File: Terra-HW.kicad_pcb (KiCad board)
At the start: 2 copper layers, 78.2 x 48.5 mm, 63 parts, among them J1 GT-USB-7010ASV, J2 S2B-PH-SM4-TB, J3 0532610271, J5 B8B-PH-SM4-TB, J6 0532610671, Q1 DMP3099L, Q2 2N7002, SW2 KMR231NG, SW3 KMR231NG, SW4 KMR231NG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

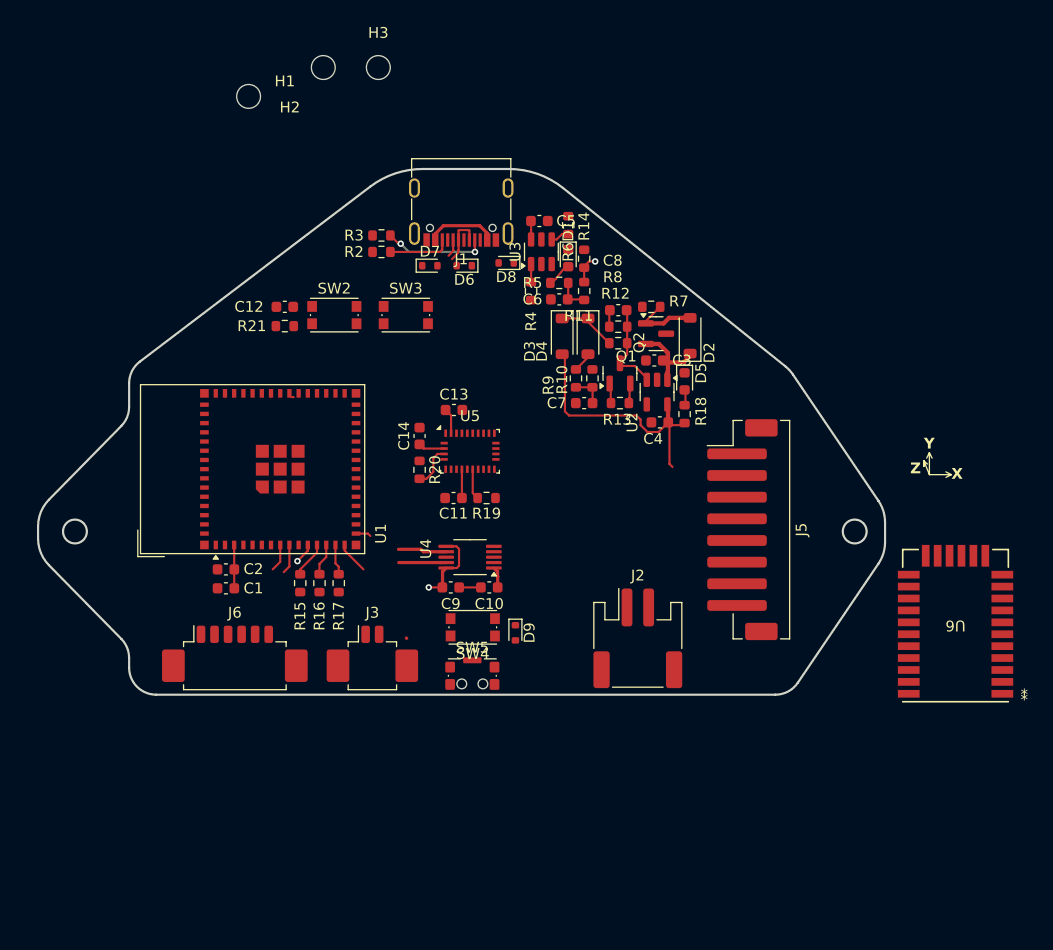
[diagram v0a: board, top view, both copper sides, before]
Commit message: Updated board outline to version 004
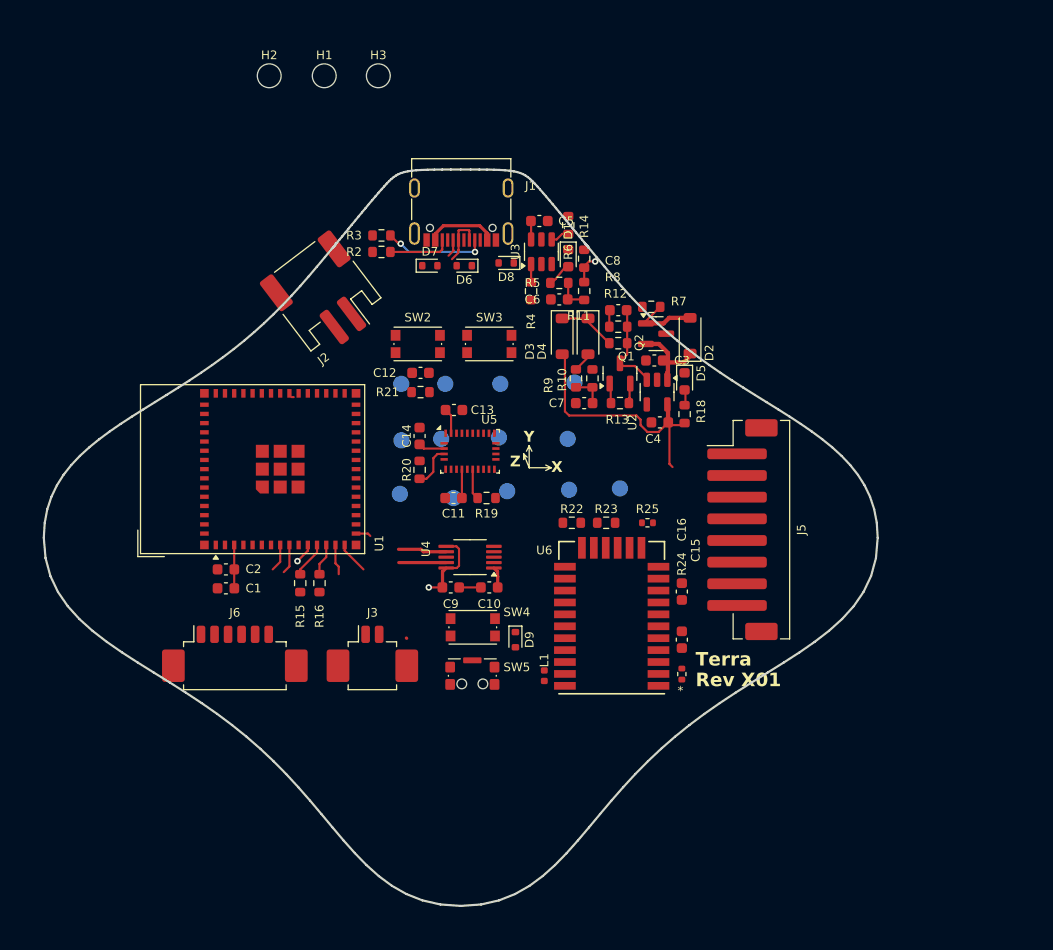
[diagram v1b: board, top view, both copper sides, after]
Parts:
- removed R17: 10k, Resistor_SMD:R_0603_1608Metric
- added C15: 22p, Capacitor_SMD:C_0603_1608Metric, F.Cu at (170.2, 115.6)
- added C16: 22p, Capacitor_SMD:C_0603_1608Metric, F.Cu at (170.2, 111.1)
- added L1: 1.8n, Inductor_SMD:L_0402_1005Metric, F.Cu at (157.5, 118.9)
- added R22: 10k, Resistor_SMD:R_0603_1608Metric, F.Cu at (160.0, 104.8)
- added R23: 10k, Resistor_SMD:R_0603_1608Metric, F.Cu at (163.2, 104.8)
- added R24: 0R, Resistor_SMD:R_0402_1005Metric, F.Cu at (170.2, 118.7)
- added R25: 0R, Resistor_SMD:R_0402_1005Metric, F.Cu at (167.0, 104.8)
- added TP1: TXD0, M20048-1:TestPoint_Pad_D1.5mm_WITH_LABEL, B.Cu at (144.3, 91.9)
- added TP10: SPI_MOSI, M20048-1:TestPoint_Pad_D1.5mm_WITH_LABEL, B.Cu at (160.3, 91.8)
- added TP11: SPI_SCK, M20048-1:TestPoint_Pad_D1.5mm_WITH_LABEL, B.Cu at (159.6, 97.0)
- added TP12: TXD0, M20048-1:TestPoint_Pad_D1.5mm_WITH_LABEL, B.Cu at (159.8, 101.7)
- added TP13: VUSB, M20048-1:TestPoint_Pad_D1.5mm_WITH_LABEL, B.Cu at (164.5, 101.6)
- added TP2: RXD0, M20048-1:TestPoint_Pad_D1.5mm_WITH_LABEL, B.Cu at (144.3, 97.2)
- added TP3: 3.3V, M20048-1:TestPoint_Pad_D1.5mm_WITH_LABEL, B.Cu at (144.1, 102.1)
- added TP4: V_SW, M20048-1:TestPoint_Pad_D1.5mm_WITH_LABEL, B.Cu at (148.3, 91.9)
- added TP5: GND, M20048-1:TestPoint_Pad_D1.5mm_WITH_LABEL, B.Cu at (148.0, 97.0)
- added TP6: GND, M20048-1:TestPoint_Pad_D1.5mm_WITH_LABEL, B.Cu at (149.1, 102.5)
- added TP7: I2C_SDA, M20048-1:TestPoint_Pad_D1.5mm_WITH_LABEL, B.Cu at (153.4, 91.9)
- added TP8: I2C_SCL, M20048-1:TestPoint_Pad_D1.5mm_WITH_LABEL, B.Cu at (153.3, 96.9)
- added TP9: SPI_CS0, M20048-1:TestPoint_Pad_D1.5mm_WITH_LABEL, B.Cu at (154.1, 101.9)
- R15, R16: value 10k -> 5.1k
- moved J2 42.9 mm to (137.2, 83.8), turned to -142.779 degrees
- moved U6 31.8 mm to (163.7, 113.5)
- moved C12 13.9 mm to (146.1, 90.9)
- moved R21 13.9 mm to (146.1, 92.7)
- moved SW3 8.15 mm to (152.4, 88.3)
- moved SW2 8.15 mm to (145.8, 88.3)
- moved H2 2.69 mm to (132.1, 63.5)
- moved H1 0.77 mm to (137.2, 63.5)
- moved H3 0.76 mm to (142.2, 63.5)
- moved D9 0.63 mm to (154.8, 115.6)
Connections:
- R15 pad 1: /Microcontroller/I2C_SDA -> +3.3V
- R15 pad 2: +3.3V -> /Microcontroller/I2C_SDA
- R16 pad 1: /Microcontroller/I2C_SCL -> +3.3V
- R16 pad 2: +3.3V -> /Microcontroller/I2C_SCL
- R19 pad 2: /Peripehrals/CMP_~{RST} -> /Microcontroller/CMP_~{RST}
- U1 pad 33: unconnected-(U1-IO37-Pad33) -> /Microcontroller/CMP_INT
- U1 pad 34: unconnected-(U1-IO38-Pad34) -> /Microcontroller/CMP_~{RST}
- U1 pad 35: unconnected-(U1-IO39-Pad35) -> /Microcontroller/GPS_~{RST}
- U1 pad 36: unconnected-(U1-IO40-Pad36) -> /Microcontroller/GPS_STBY
- U1 pad 37: unconnected-(U1-IO41-Pad37) -> /Microcontroller/CMP_FIX
- U1 pad 39: unconnected-(U1-TXD0-Pad39) -> /Microcontroller/TXD0
- U1 pad 40: unconnected-(U1-RXD0-Pad40) -> /Microcontroller/RXD0
- U1 pad 7: /Microcontroller/CMP_INT -> unconnected-(U1-IO3-Pad7)
- U5 pad 11: /Peripehrals/CMP_~{RST} -> /Microcontroller/CMP_~{RST}
- U6 pad 1: unconnected-(U6-AT1-Pad1) -> Net-(U6-AT1)
- U6 pad 10: unconnected-(U6-~{HW_RST}-Pad10) -> /Microcontroller/GPS_~{RST}
- U6 pad 12: unconnected-(U6-BV-Pad12) -> /Peripehrals/GPS_VBACKUP
- U6 pad 13: unconnected-(U6-E2-Pad13) -> /Peripehrals/GPS_BAUD1
- U6 pad 14: unconnected-(U6-E3-Pad14) -> /Peripehrals/GPS_BAUD2
- U6 pad 15: Net-(U6-GND-Pad15) -> GND
- U6 pad 16: Net-(U6-GND-Pad15) -> GND
- U6 pad 17: Net-(U6-GND-Pad15) -> GND
- U6 pad 18: unconnected-(U6-FIX-Pad18) -> /Microcontroller/CMP_FIX
- U6 pad 19: Net-(U6-GND-Pad15) -> GND
- U6 pad 2: Net-(U6-GND-Pad2) -> GND
- U6 pad 20: unconnected-(U6-TX-Pad20) -> /Microcontroller/U1RXD
- U6 pad 21: unconnected-(U6-RX-Pad21) -> /Microcontroller/U1TXD
- U6 pad 22: Net-(U6-GND-Pad15) -> GND
- U6 pad 23: Net-(U6-GND-Pad15) -> GND
- U6 pad 24: Net-(U6-GND-Pad15) -> GND
- U6 pad 25: Net-(U6-GND-Pad15) -> GND
- U6 pad 26: unconnected-(U6-HW_STBY-Pad26) -> /Microcontroller/GPS_STBY
- U6 pad 27: Net-(U6-GND-Pad15) -> GND
- U6 pad 28: unconnected-(U6-AT2-Pad28) -> Net-(U6-AT2)
- U6 pad 3: Net-(U6-GND-Pad2) -> GND
- U6 pad 4: unconnected-(U6-ANT_OUT-Pad4) -> Net-(U6-ANT_OUT)
- U6 pad 5: Net-(U6-GND-Pad2) -> GND
- U6 pad 6: unconnected-(U6-RF_IN-Pad6) -> Net-(U6-RF_IN)
- U6 pad 7: Net-(U6-GND-Pad2) -> GND
- U6 pad 8: unconnected-(U6-VCC-Pad8) -> +3.3V
- U6 pad 9: Net-(U6-GND-Pad2) -> GND
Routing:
- net /Peripehrals/CMP_~{RST}: track 2.84 -> 0.00 mm
- net /Microcontroller/CMP_~{RST}: track 0.00 -> 2.84 mm
- added copper zone on In2.Cu, net +3.3V
- added copper zone on In1.Cu, net GND
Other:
- board size 78.2 x 48.5 mm -> 77 x 68 mm
- copper layers 2 -> 4
- board text added: "${TITLE}"
- board text added: "Rev ${REVISION}"

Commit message: Component placement for -004 board outline.
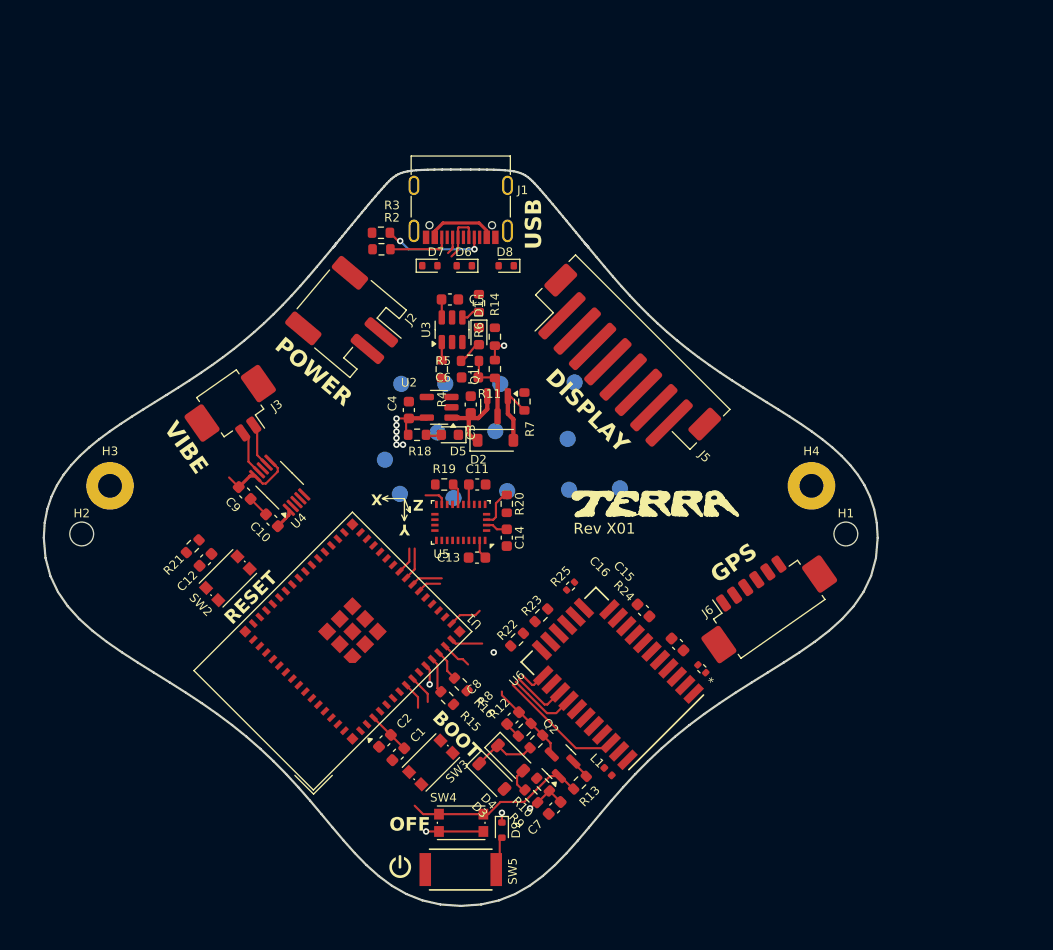
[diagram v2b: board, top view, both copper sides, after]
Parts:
- added H4: Plated Hole M2, MountingHole:MountingHole_2.2mm_M2_Pad, F.Cu at (182.1, 101.4)
- H3: value Hole M2 -> Plated Hole M2; footprint MountingHole:MountingHole_2.2mm_M2 -> MountingHole:MountingHole_2.2mm_M2_Pad
- SW5: value CK_KMS2xxGP -> KSS3xxGx; footprint Button_Switch_SMD:SW_SPST_CK_KMS2xxGP -> C&K:SW_KSS323_CNK
- moved H1 64.1 mm to (185.3, 105.8)
- moved J6 49.3 mm to (178.0, 112.4), turned to 35 degrees
- moved H2 45.7 mm to (114.8, 105.8)
- moved H3 45.2 mm to (117.4, 101.4)
- moved D3 41.1 mm to (152.6, 128.2), turned to -45 degrees
- moved D4 39.6 mm to (154.4, 126.5), turned to -45 degrees
- moved SW3 39.0 mm to (147.0, 126.9), turned to -135 degrees
- moved C8 38.9 mm to (154.6, 122.8), turned to -135 degrees
- moved R9 38.8 mm to (156.3, 130.0), turned to 135 degrees
- moved R8 38.2 mm to (155.7, 123.9), turned to -135 degrees
- moved R10 37.8 mm to (157.4, 129.0), turned to 135 degrees
- moved R12 37.5 mm to (156.7, 125.0), turned to 45 degrees
- moved C7 37.5 mm to (158.4, 131.1), turned to -135 degrees
- moved Q2 36.3 mm to (158.8, 126.8), turned to 135 degrees
- moved R13 35.2 mm to (160.8, 128.8), turned to -135 degrees
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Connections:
- U6 pad 18: /Microcontroller/CMP_FIX -> /Microcontroller/GPS_FIX
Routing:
- net +3.3V: track 40.1 -> 24.8 mm, vias 1 -> 8
- net /Microcontroller/PWROFF: track 1.86 -> 16.9 mm
- net /Microcontroller/GPS_STBY: track 0.00 -> 11.7 mm
- net /Microcontroller/U1TXD: track 0.00 -> 8.76 mm
- net /Microcontroller/U1RXD: track 0.00 -> 8.20 mm
- net VBAT: track 3.34 -> 7.25 mm
- net Net-(D4-A): track 2.16 -> 5.58 mm
- net /Microcontroller/DATA-: track 5.15 -> 8.20 mm
- net /Microcontroller/GPS_FIX: track 0.00 -> 2.66 mm
- net /Microcontroller/DATA+: track 1.65 -> 4.14 mm
- net /Microcontroller/CMP_INT: track 0.00 -> 2.18 mm
- net /Microcontroller/SPI_SCK: track 1.41 -> 3.08 mm
- net /Microcontroller/PWR_SW: track 2.99 -> 3.91 mm, vias 0 -> 1
- net GND: track 5.51 -> 6.41 mm, vias 0 -> 1
- net /Microcontroller/CMP_~{RST}: track 2.84 -> 2.02 mm
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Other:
- board text added: "BOOT"
- board text added: "DISPLAY"
- board text added: "GPS"
- board text added: "OFF"
- board text added: "POWER"
- board text added: "RESET"
- board text added: "USB"
- board text added: "VIBE"
- board text removed: "${TITLE}"

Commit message: Lots of board layout
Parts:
- added C17: 0.1u, Capacitor_SMD:C_0603_1608Metric, F.Cu at (155.0, 100.7)
- added C18: 0.1u, Capacitor_SMD:C_0603_1608Metric, F.Cu at (146.1, 122.7)
- added C19: 1u, Capacitor_SMD:C_0603_1608Metric, F.Cu at (176.9, 107.1)
- added D10: GPIO48, Diode_SMD:D_0603_1608Metric, F.Cu at (135.6, 105.9)
- added D11: MBR0520, Diode_SMD:D_SOD-123, F.Cu at (158.9, 99.3)
- added FID1: Fiducial, Fiducial:Fiducial_1mm_Mask2mm, F.Cu at (185.3, 102.2)
- added FID2: Fiducial, Fiducial:Fiducial_1mm_Mask2mm, F.Cu at (156.8, 135.2)
- added FID3: Fiducial, Fiducial:Fiducial_1mm_Mask2mm, F.Cu at (114.3, 102.2)
- added Q3: 2N7002, Package_TO_SOT_SMD:SOT-23, F.Cu at (158.1, 93.1)
- added R17: 10k, Resistor_SMD:R_0603_1608Metric, F.Cu at (157.7, 95.9)
- added R26: 1.5k, Resistor_SMD:R_0603_1608Metric, F.Cu at (137.8, 103.8)
- added R27: 100k, Resistor_SMD:R_0603_1608Metric, F.Cu at (157.7, 97.4)
- added R28: 100k, Resistor_SMD:R_0603_1608Metric, F.Cu at (155.0, 99.2)
- added R29: 100k, Resistor_SMD:R_0603_1608Metric, F.Cu at (152.0, 99.2)
- moved TP7 33.8 mm to (147.3, 125.2)
- moved TP8 25.9 mm to (150.8, 122.2)
- moved TP13 25.3 mm to (147.8, 82.7)
- moved TP6 23.4 mm to (128.3, 113.2)
- moved TP1 21.7 mm to (131.8, 109.7)
- moved TP3 16.0 mm to (144.3, 86.2)
- moved TP5 15.7 mm to (163.3, 97.7)
- moved TP12 13.7 mm to (150.3, 111.7)
- moved TP9 12.0 mm to (163.3, 94.2)
- moved TP2 10.4 mm to (135.3, 106.2)
- moved TP4 7.91 mm to (140.8, 89.7)
- moved TP11 7.33 mm to (163.3, 90.7)
- moved R21 7.26 mm to (128.8, 113.2), turned to 45 degrees
- moved TP10 5.54 mm to (163.3, 87.2)
- moved C12 5.51 mm to (131.0, 111.0)
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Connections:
- net /Microcontroller/DISP_RST renamed /Microcontroller/DISP_~{RST}
- net /Microcontroller/RXD0 renamed /Microcontroller/U0RXD
- net /Microcontroller/SPI_~{CS0} renamed /Microcontroller/SPI_~{CS0_DISP}
- net /Microcontroller/TXD0 renamed /Microcontroller/U0TXD
- U1 pad 10: /Microcontroller/HAPTIC_IN_TRG -> unconnected-(U1-RTC_GPIO6/GPIO6/TOUCH6/ADC1_CH5-Pad10)
- U1 pad 11: /Microcontroller/VBAT_OVER_2 -> unconnected-(U1-RTC_GPIO7/GPIO7/TOUCH7/ADC1_CH6-Pad11)
- U1 pad 30: unconnected-(U1-IO48-Pad30) -> /Microcontroller/LED_GPIO48
- U1 pad 37: /Microcontroller/CMP_FIX -> /Microcontroller/GPS_FIX
- U1 pad 38: unconnected-(U1-IO42-Pad38) -> /Microcontroller/HAPTIC_IN_TRG
- U1 pad 5: unconnected-(U1-IO1-Pad5) -> /Microcontroller/VBAT_OVER_2
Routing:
- net /Microcontroller/I2C_SCL: track 2.96 -> 69.6 mm, vias 0 -> 4
- net /Microcontroller/I2C_SDA: track 3.34 -> 68.3 mm, vias 0 -> 5
- net V_SW: track 7.49 -> 69.7 mm, vias 0 -> 2
- net /Microcontroller/VBAT_OVER_2: track 4.07 -> 58.1 mm
- net /Microcontroller/DISP_~{RST}: track 2.54 -> 50.4 mm, vias 0 -> 2
- net Net-(D11-K): track 6.14 -> 51.0 mm, vias 0 -> 2
- net /Power/PWR_EN: track 7.94 -> 52.3 mm
- net /Microcontroller/PWR_SW: track 3.91 -> 43.2 mm, vias 1 -> 2
- net /Microcontroller/U1TXD: track 8.76 -> 47.0 mm, vias 0 -> 4
- net /Microcontroller/U1RXD: track 8.20 -> 46.2 mm, vias 0 -> 4
- net /Microcontroller/SPI_MOSI: track 2.98 -> 39.1 mm, vias 0 -> 2
- net /Microcontroller/GPS_~{RST}: track 0.00 -> 35.8 mm, vias 0 -> 2
- net /Microcontroller/DATA+: track 4.14 -> 39.8 mm
- net /Microcontroller/DISP_PWM_BL: track 2.73 -> 38.0 mm, vias 0 -> 2
- net /Microcontroller/PWROFF: track 16.9 -> 50.9 mm, vias 0 -> 2
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- added copper zone on F.Cu, net +3.3V
- added copper zone on F.Cu, net GND
- added copper zone on F.Cu, net VBAT
- added copper zone on In2.Cu, net VBAT
- added copper zone on F.Cu, net VUSB
- added copper zone on In2.Cu, net VUSB
- added copper zone on F.Cu, net V_SW
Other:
- board text added: "Rev. ${REVISION}"
- board text added: "© ${COPYRIGHT} Modem and Panter & Tourron"
- board text removed: "BOOT"
- board text removed: "DISPLAY"
- board text removed: "GPS"
- board text removed: "OFF"
- board text removed: "POWER"
- board text removed: "RESET"
- board text removed: "Rev ${REVISION}"
- board text removed: "USB"
- board text removed: "VIBE"

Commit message: More layout and sch updates, ready for final review.
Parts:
- D11, D2, D3, D4: value MBR0520 -> PMEG2010AEH
- D6, D7, D8, D9: value ESD5B5.0ST1G -> DESD5V0U1BB-7
- moved TP8 7.00 mm to (143.8, 122.2)
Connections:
- R17 pad 2: V_USB -> VUSB
- R27 pad 1: V_USB -> VUSB
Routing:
- net GND: track 25.3 -> 39.3 mm, vias 13 -> 66
- net /Microcontroller/I2C_SCL: track 69.6 -> 79.6 mm, vias 4 -> 5
- net /Microcontroller/U0RXD: track 0.00 -> 9.61 mm, vias 0 -> 1
- net /Microcontroller/SPI_~{CS0_DISP}: track 34.5 -> 31.8 mm
- net /Microcontroller/U0TXD: track 0.00 -> 2.27 mm, vias 0 -> 1
- net /Microcontroller/DISP_DC: track 32.8 -> 30.6 mm
- net +3.3V: track 44.3 -> 42.2 mm
- net /Microcontroller/GPS_STBY: track 36.5 -> 34.5 mm
- net /Microcontroller/SPI_MOSI: track 39.1 -> 37.3 mm
- net V_SW: track 69.7 -> 67.9 mm
- net /Microcontroller/GPS_~{RST}: track 35.8 -> 34.5 mm
- net /Power/PWR_EN: track 52.3 -> 51.0 mm
- net /Microcontroller/GPS_FIX: track 28.0 -> 26.9 mm
- net /Microcontroller/HAPTIC_IN_TRG: track 12.7 -> 11.6 mm
- net Net-(Q3-G): track 9.03 -> 8.00 mm
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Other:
- board text added: "+"
- board text added: "-"
- board text added: "0"
- board text added: "0 mm"
- board text added: "0.01 mm"
- board text added: "0.0152 mm"
- board text added: "0.02"
- board text added: "0.035 mm"
- board text added: "0.0994 mm"
- board text added: "0.1500 mm / 0.1500 mm"
- board text added: "0.2000 mm"
- board text added: "1"
- board text added: "1.265 mm"
- board text added: "1.5842 mm"
- board text added: "3.3"
- board text added: "4"
- board text added: "4.5"
- board text added: "77.0000 mm x 68.0000 mm"
- board text added: "B.Cu"
- board text added: "B.Mask"
- board text added: "B.Paste"
- board text added: "B.Silkscreen"
- board text added: "BOARD CHARACTERISTICS"
- board text added: "Black"
- board text added: "Board Thickness:"
- board text added: "Board overall dimensions:"
- board text added: "Bottom Silk Screen"
- board text added: "Bottom Solder Mask"
- board text added: "Bottom Solder Paste"
- board text added: "Castellated pads:"
- board text added: "Color"
- board text added: "Copper Finish:"
- board text added: "Copper Layer Count:"
- board text added: "Dielectric"
- board text added: "Edge card connectors:"
- board text added: "Epsilon R"
- board text added: "F.Cu"
- board text added: "F.Mask"
- board text added: "F.Paste"
- board text added: "F.Silkscreen"
- board text added: "FR4"
- board text added: "Impedance Control:"
- board text added: "In1.Cu"
- board text added: "In2.Cu"
- board text added: "Layer Name"
- board text added: "Loss Tangent"
- board text added: "Material"
- board text added: "Min hole diameter:"
- board text added: "Min track/spacing:"
- board text added: "NOT ALL THOSE WHO WANDER ARE LOST"
- board text added: "No"
- board text added: "None"
- board text added: "Not specified"
- board text added: "Plated Board Edge:"
- board text added: "Thickness (mm)"
- board text added: "Top Silk Screen"
- board text added: "Top Solder Mask"
- board text added: "Top Solder Paste"
- board text added: "Type"
- board text added: "White"
- board text added: "copper"
- board text added: "core"
- board text added: "prepreg"
- board text removed: "© ${COPYRIGHT} Modem and Panter & Tourron"
